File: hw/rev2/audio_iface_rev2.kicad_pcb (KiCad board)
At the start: 4 copper layers, 66 x 24.8 mm, 145 parts, among them J1 COAX, J2 CONN_2, J3 USBMICROCONN, J4 CONN_2, J5 CONN_2, J6 COAX, J7 COAX, J8 CONN_6, J9 CONN_2, U1 LT6241, U2 LTC6242, U3 AK4621, U4 K20X7_QFP64, U5 TPS61252, U6 LP2992AILD-5.0, U7 LTC6242, U8 TPA6130A2, U9 MT29FXX01A, X1 XTAL, X2 ASFLM2-12.288MHZ

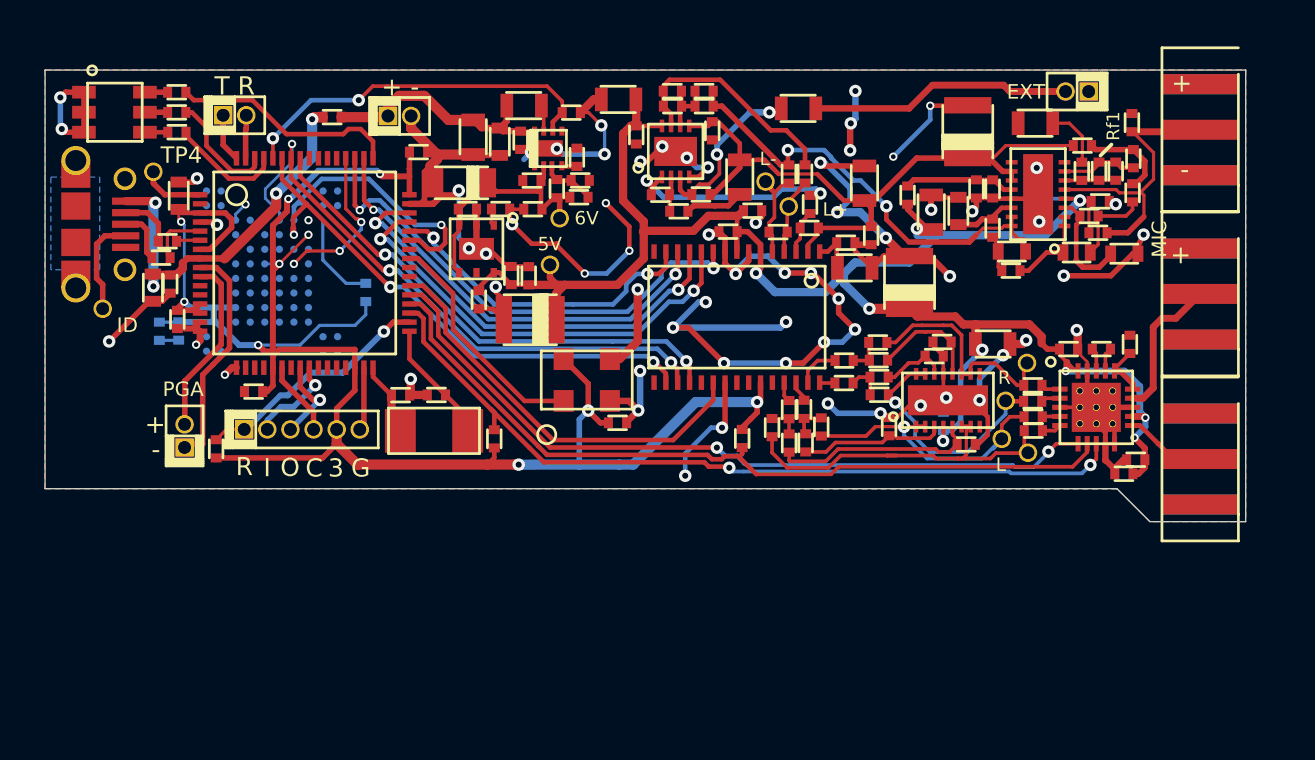
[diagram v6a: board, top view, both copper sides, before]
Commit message: Started board upgrade to 4 layers and better signal isolation
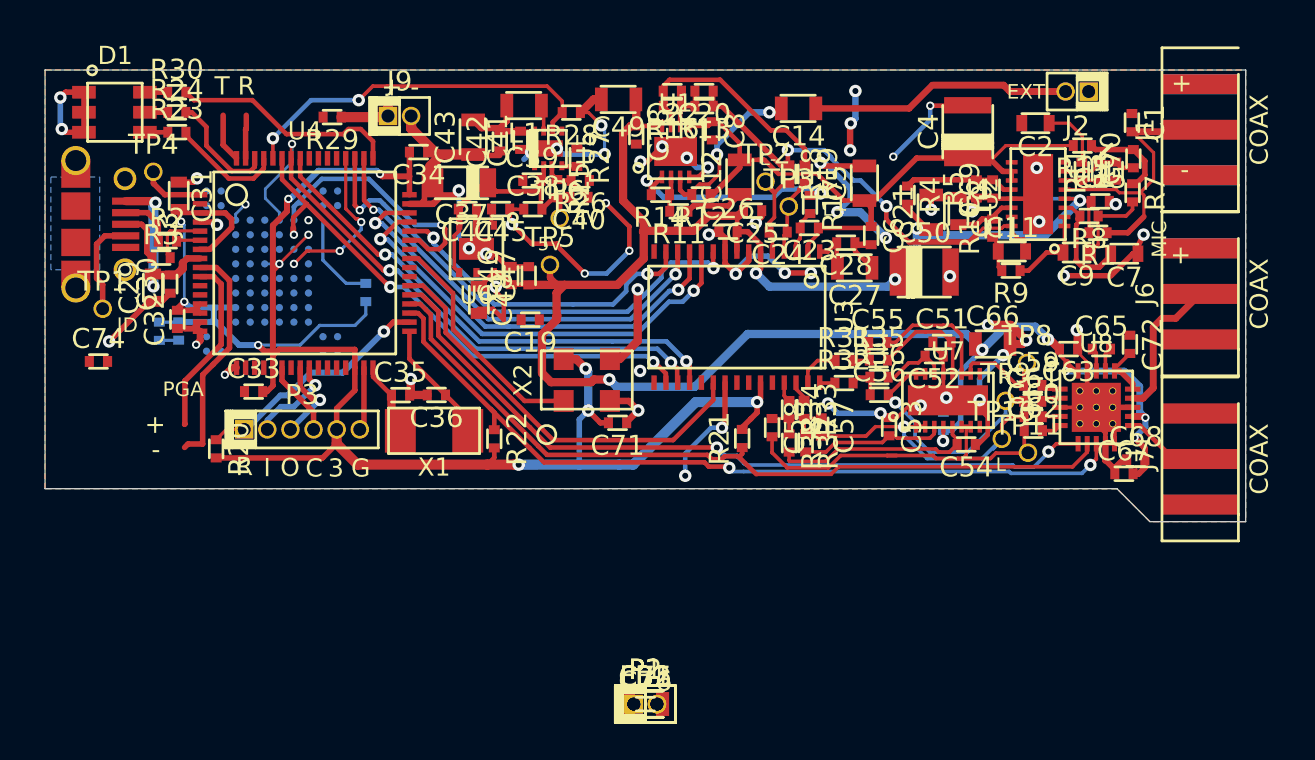
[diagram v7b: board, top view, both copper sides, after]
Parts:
- removed J4, J5: CONN_2, HDR_2X1_50MIL
- removed J8: CONN_6, HDR_6X1_50MIL
- added C74: 47p, lib:SMD0402, F.Cu at (154.9, 88.0)
- added C75: 10u, lib:SMD0805, F.Cu at (185.0, 106.8)
- added C76: 0.1u, lib:SMD0402, F.Cu at (185.0, 106.8)
- added FB1, FB2: BLM18PG221SN1D, lib:SMD0805, F.Cu at (185.0, 106.8)
- added P1, P2: CONN_01X02, lib:HDR_2X1_50MIL, F.Cu at (185.0, 106.8)
- added P3: CONN_01X06, lib:HDR_6X1_50MIL, F.Cu at (166.1, 91.7)
- C1, C13, C15, C16, C17, C18, C20, C22, C23, C24, C25, C26, C28, C3, C30, C32, C33, C34, C35, C36, C38, C39, C40, C41, C44, C45, C46, C47, C51, C52, C53, C54, C55, C56, C57, C58, C59, C6, C60, C61, C62, C63, C64, C65, C67, C68, C69, C70, C71, C72, C73, C8, R1, R10, R11, R12, R13, R14, R15, R16, R17, R18, R19, R2, R20, R21, R22, R23, R24, R25, R26, R27, R28, R29, R3, R30, R31, R32, R33, R34, R35, R36, R37, R38, R39, R4, R5, R6, R7, R8, R9, Rf1: footprint SMD0402 -> lib:SMD0402
- C10, C11, C29, C31, C7, C9: footprint SMD0603 -> lib:SMD0603
- C12, C14, C21, C27, C43, C49, C5, C66, L1: footprint SMD0805 -> lib:SMD0805
- C19: footprint SMD1411_POL -> lib:SMD0402
- C2: footprint SMD0805 -> lib:SMD0603
- C37: footprint SMD1206_POL -> lib:SMD1206_POL
- C4, C50: footprint SMD1411_POL -> lib:SMD1411_POL
- C42: footprint SMD0603 -> lib:SMD0402
- C48: footprint SMD0402 -> lib:SMD0603
- D1: footprint LED-6PLCC -> lib:LED-6PLCC
- J1, J6, J7: footprint SMA_EDGE -> lib:SMA_EDGE
- J2, J9: value CONN_2 -> CONN_01X02; footprint HDR_2X1_50MIL -> lib:HDR_2X1_50MIL
- J3: footprint FCI_10118194 -> lib:FCI_10118194
- TP1, TP10, TP11, TP2, TP3, TP4, TP5, TP6, TP8, TP9: footprint TP_HOLE -> lib:TP_HOLE
- U1: footprint LT_DFN8_DUAL -> lib:LT_DFN8_DUAL
- U2, U7: footprint LT_DFN16_QUAD -> lib:LT_DFN16_QUAD
- U3: footprint AK4621_VSOP30 -> lib:AK4621_VSOP30
- U4: footprint FREESCALE_QFP64 -> lib:FREESCALE_QFP64
- U5: footprint TPS61252_QFN8 -> lib:TPS61252_QFN8
- U6: footprint TI_WSON6 -> lib:TI_WSON6
- U8: footprint TPA8130A2-QFN20 -> lib:TPA8130A2-QFN20
- U9: footprint MICRON_VFBGA63 -> MICRON_VFBGA63:MICRON_VFBGA63
- X1: footprint TXC_7A -> lib:TXC_7A
- X2: footprint ASFLM -> lib:ASFLM
- moved C50 0.99 mm to (200.3, 83.1), turned to 0 degrees
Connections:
- J3 pad 1: USB_5V -> Net-(C75-Pad1)
- J3 pad 5: AGND_IN -> Net-(FB1-Pad1)
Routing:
- net AGND_IN: track 216.9 -> 188.5 mm, vias 64 -> 56
- net +5VA: track 103.9 -> 123.4 mm, vias 9 -> 11
- net USB_5V: track 24.0 -> 10.9 mm, vias 4 -> 2
- net Net-(C41-Pad2): track 13.6 -> 8.02 mm
- net Net-(C75-Pad1): track 0.00 -> 1.55 mm
- net +3V: track 110.3 -> 110.7 mm, vias 10 -> 11
- net (no net): vias 3 -> 4

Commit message: Routed out 4-layer variant--now need to do silkscreens and such
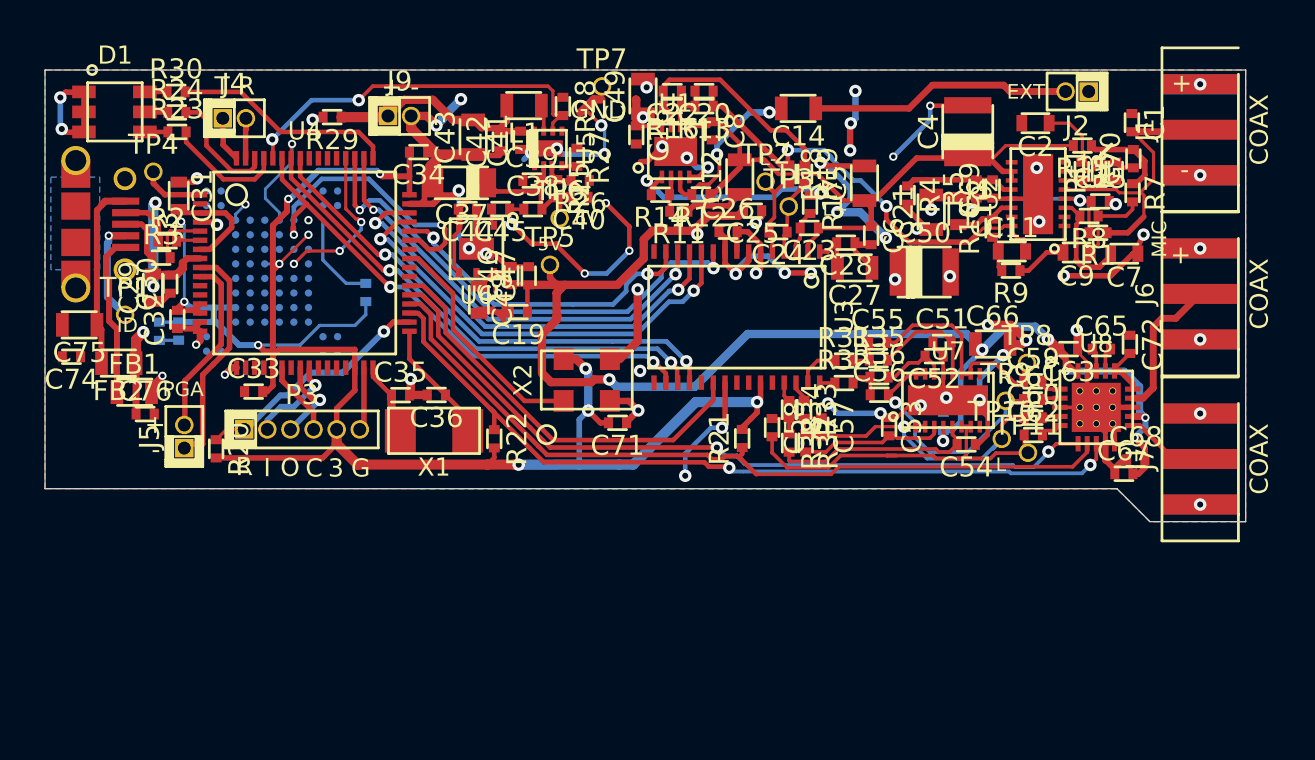
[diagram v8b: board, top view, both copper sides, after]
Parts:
- removed P1, P2: CONN_01X02, lib:HDR_2X1_50MIL
- added J4: CONN_01X02, lib:HDR_2X1_50MIL, F.Cu at (162.4, 74.7)
- added J5: CONN_01X02, lib:HDR_2X1_50MIL, F.Cu at (159.7, 92.1)
- added TP7: TP, lib:TP_HOLE, F.Cu at (182.6, 72.9)
- moved C75 37.4 mm to (153.9, 86.0), turned to 180 degrees
- moved FB2 34.5 mm to (156.1, 88.1), turned to 180 degrees
- moved FB1 32.9 mm to (156.9, 89.7)
- moved C76 31.8 mm to (157.5, 90.9)
- moved C74 1.50 mm to (153.4, 87.8), turned to 180 degrees
- moved C49 1.35 mm to (184.8, 73.5), turned to 90 degrees
- moved TP1 1.28 mm to (156.4, 85.5)
- moved C19 0.78 mm to (178.0, 85.3)
- moved R28 0.57 mm to (180.4, 74.0), turned to 270 degrees
- moved C62 0.24 mm to (206.3, 92.0)
- moved C59 0.22 mm to (206.3, 89.1)
- moved C61 0.10 mm to (206.3, 90.1)
- moved C60 0.05 mm to (206.3, 91.1)
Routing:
- net AGND_IN: track 188.5 -> 199.1 mm, vias 56 -> 63
- net Net-(C75-Pad1): track 1.55 -> 11.7 mm
- net Net-(FB1-Pad1): track 0.00 -> 8.98 mm
- net Net-(C41-Pad2): track 8.02 -> 13.5 mm
- net USB_5V: track 10.9 -> 16.2 mm, vias 2 -> 4
- net +5VA: track 123.4 -> 124.4 mm, vias 11 -> 13
- net Net-(J3-Pad4): track 5.48 -> 5.72 mm, vias 0 -> 1
- added copper zone on Inner1.Cu, net +5VA
- added copper zone on Inner1.Cu, net USB_5V
- removed copper zone on Inner1.Cu, net AGND_IN
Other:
- board text added: "GND"
